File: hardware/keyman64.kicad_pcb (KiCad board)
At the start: 2 copper layers, 80 x 64.7 mm, 36 parts, among them J1 POWER, P1 COMPUTER, P2 KEYBOARD, P3 USB, P4 SERIAL, P5 CONTROL, SW1 RESET, SW2 BOOT, U1 CD74HC22106/MT8808, U2 ATMEGA1284P-PU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

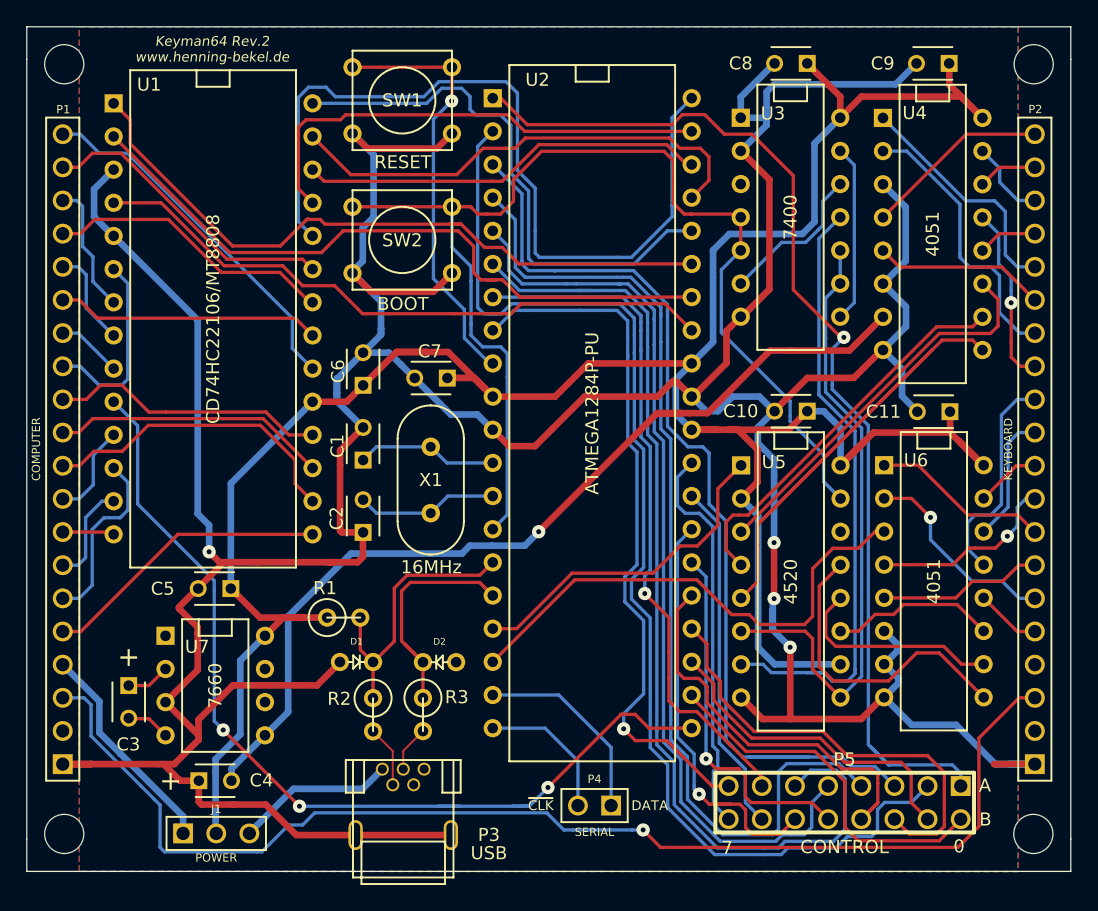
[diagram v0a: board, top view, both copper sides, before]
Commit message: Hardware: Increased mounting hole size to 4mm
This was self-adhesive pcb holders like reichelts AHS 4,8 may be used
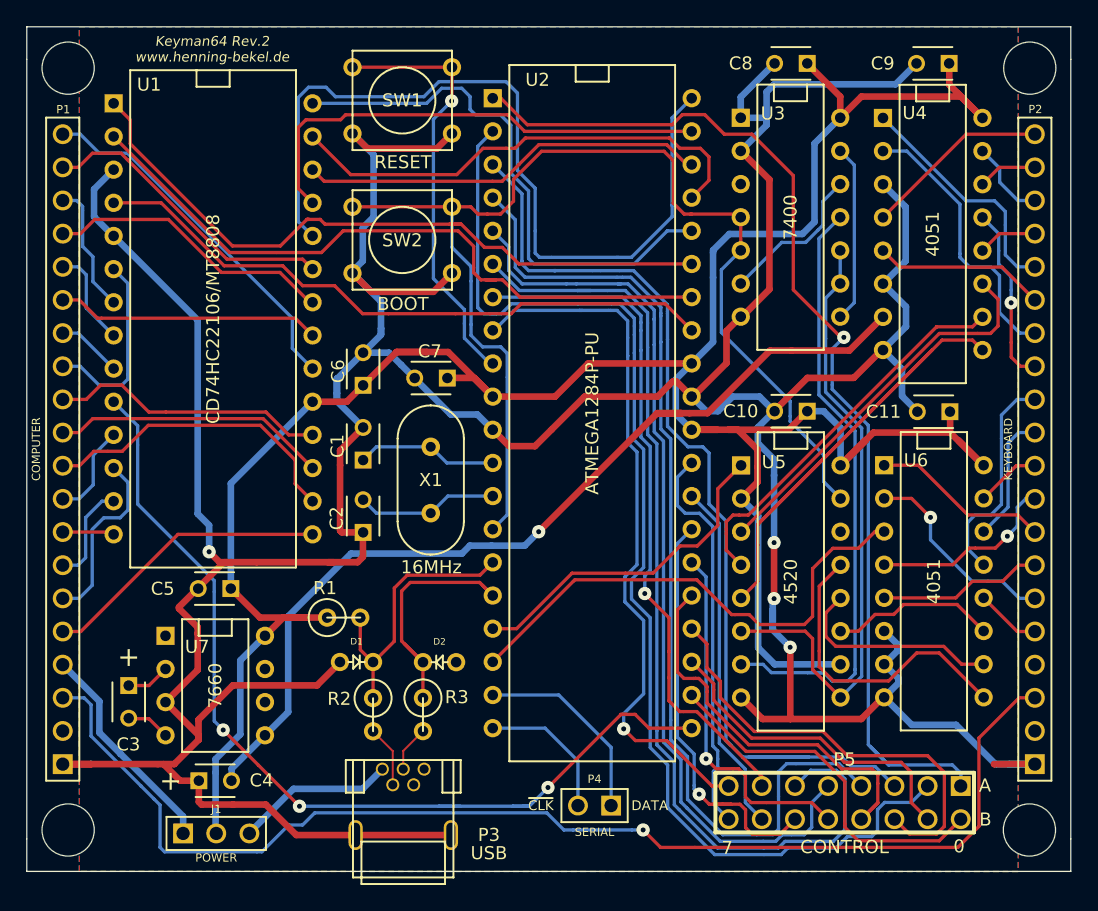
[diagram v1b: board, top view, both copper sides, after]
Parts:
- H1, H2, H3, H4: footprint Mounting_Holes:MountingHole_3mm -> Mounting_Holes:MountingHole_4mm
- moved H4 0.42 mm to (181.5, 69.5), turned to 180 degrees
- moved H1 0.42 mm to (107.8, 127.9)
- moved H3 0.42 mm to (107.8, 69.5)
- moved H2 0.42 mm to (181.4, 127.9)
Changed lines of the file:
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@@
     (area 104.572599 66.320199 184.657201 131.126701)
     (thickness 1.6)
-    (drawings 20)
+    (drawings 19)
     (tracks 1192)
     (zones 0)
@@
     (mod_text_size 1 1)
     (mod_text_width 0.15)
-    (pad_size 3.2 3.2)
-    (pad_drill 3.2)
+    (pad_size 4 4)
+    (pad_drill 4)
     (pad_to_mask_clearance 0)
     (aux_axis_origin 0 0)
@@
     (add_net /D-)
   )
-  (module Mounting_Holes:MountingHole_3mm (layer F.Cu)
-    (at 107.4928 128.2065)
-    (descr "Mounting hole, Befestigungsbohrung, 3mm, No Annular, Kein Restring,")
-    (tags "Mounting hole, Befestigungsbohrung, 3mm, No Annular, Kein Restring,")
-    (fp_text reference H1 (at 0.1524 -0.1778) (layer Dwgs.User) hide
-      (effects (font (size 1 1) (thickness 0.15)))
-    )
-    (fp_text value CONN_1 (at 1.00076 5.00126) (layer Dwgs.User) hide
-      (effects (font (size 1 1) (thickness 0.15)))
-    )
-    (fp_circle (center 0 0) (end 3 0) (layer Cmts.User) (width 0.381))
-    (pad 1 thru_hole circle (at 0 0) (size 3 3) (drill 3) (layers)
-      (net 83 "Net-(H1-Pad1)"))
-  )
-  (module Mounting_Holes:MountingHole_3mm (layer F.Cu)
-    (at 181.737 128.2065)
-    (descr "Mounting hole, Befestigungsbohrung, 3mm, No Annular, Kein Restring,")
-    (tags "Mounting hole, Befestigungsbohrung, 3mm, No Annular, Kein Restring,")
-    (fp_text reference H2 (at 0.1397 -0.1016) (layer Dwgs.User) hide
-      (effects (font (size 1 1) (thickness 0.15)))
-    )
-    (fp_text value CONN_1 (at 1.00076 5.00126) (layer Dwgs.User) hide
-      (effects (font (size 1 1) (thickness 0.15)))
-    )
-    (fp_circle (center 0 0) (end 3 0) (layer Cmts.User) (width 0.381))
-    (pad 1 thru_hole circle (at 0 0) (size 3 3) (drill 3) (layers)
-      (net 84 "Net-(H2-Pad1)"))
-  )
-  (module Mounting_Holes:MountingHole_3mm (layer F.Cu)
-    (at 107.4928 69.2404)
-    (descr "Mounting hole, Befestigungsbohrung, 3mm, No Annular, Kein Restring,")
-    (tags "Mounting hole, Befestigungsbohrung, 3mm, No Annular, Kein Restring,")
-    (fp_text reference H3 (at -0.0254 -0.0889) (layer Dwgs.User) hide
-      (effects (font (size 1 1) (thickness 0.15)))
-    )
-    (fp_text value CONN_1 (at -0.0254 -3.8354) (layer Dwgs.User) hide
-      (effects (font (size 1 1) (thickness 0.15)))
-    )
-    (fp_circle (center 0 0) (end 3 0) (layer Cmts.User) (width 0.381))
-    (pad 1 thru_hole circle (at 0 0) (size 3 3) (drill 3) (layers)
-      (net 85 "Net-(H3-Pad1)"))
-  )
-  (module Mounting_Holes:MountingHole_3mm (layer F.Cu)
-    (at 181.7624 69.2404)
-    (descr "Mounting hole, Befestigungsbohrung, 3mm, No Annular, Kein Restring,")
-    (tags "Mounting hole, Befestigungsbohrung, 3mm, No Annular, Kein Restring,")
-    (fp_text reference H4 (at 0.0762 -0.1397) (layer Dwgs.User) hide
-      (effects (font (size 1 1) (thickness 0.15)))
-    )
-    (fp_text value CONN_1 (at 0.3175 -4.0894) (layer Dwgs.User) hide
-      (effects (font (size 1 1) (thickness 0.15)))
-    )
-    (fp_circle (center 0 0) (end 3 0) (layer Cmts.User) (width 0.381))
-    (pad 1 thru_hole circle (at 0 0) (size 3 3) (drill 3) (layers)
-      (net 86 "Net-(H4-Pad1)"))
-  )
   (module Capacitors_ThroughHole:C_Disc_D3_P2.5 (layer F.Cu)
     (at 164.4142 69.1769 180)
@@
     )
   )
+  (module Mounting_Holes:MountingHole_4mm (layer F.Cu)
+    (at 107.7928 127.9065)
+    (descr "Mounting Hole 4mm, no annular")
+    (tags "mounting hole 4mm no annular")
+    (fp_text reference H1 (at 0.1572 6.5865) (layer F.SilkS) hide
+      (effects (font (size 1 1) (thickness 0.15)))
+    )
+    (fp_text value CONN_1 (at 0 5) (layer F.Fab)
+      (effects (font (size 1 1) (thickness 0.15)))
+    )
+    (fp_circle (center 0 0) (end 4 0) (layer Cmts.User) (width 0.15))
+    (fp_circle (center 0 0) (end 4.25 0) (layer F.CrtYd) (width 0.05))
+    (pad 1 np_thru_hole circle (at 0 0) (size 4 4) (drill 4) (layers *.Cu *.Mask F.SilkS)
+      (net 83 "Net-(H1-Pad1)"))
+  )
+  (module Mounting_Holes:MountingHole_4mm (layer F.Cu)
+    (at 181.437 127.9065)
+    (descr "Mounting Hole 4mm, no annular")
+    (tags "mounting hole 4mm no annular")
+    (fp_text reference H2 (at 0.173 6.5865) (layer F.SilkS) hide
+      (effects (font (size 1 1) (thickness 0.15)))
+    )
+    (fp_text value CONN_1 (at 0 5) (layer F.Fab)
+      (effects (font (size 1 1) (thickness 0.15)))
+    )
+    (fp_circle (center 0 0) (end 4 0) (layer Cmts.User) (width 0.15))
+    (fp_circle (center 0 0) (end 4.25 0) (layer F.CrtYd) (width 0.05))
+    (pad 1 np_thru_hole circle (at 0 0) (size 4 4) (drill 4) (layers *.Cu *.Mask F.SilkS)
+      (net 84 "Net-(H2-Pad1)"))
+  )
+  (module Mounting_Holes:MountingHole_4mm (layer F.Cu)
+    (at 107.7928 69.5404)
+    (descr "Mounting Hole 4mm, no annular")
+    (tags "mounting hole 4mm no annular")
+    (fp_text reference H3 (at 0 -5) (layer F.SilkS) hide
+      (effects (font (size 1 1) (thickness 0.15)))
+    )
+    (fp_text value CONN_1 (at 0 5) (layer F.Fab)
+      (effects (font (size 1 1) (thickness 0.15)))
+    )
+    (fp_circle (center 0 0) (end 4 0) (layer Cmts.User) (width 0.15))
+    (fp_circle (center 0 0) (end 4.25 0) (layer F.CrtYd) (width 0.05))
+    (pad 1 np_thru_hole circle (at 0 0) (size 4 4) (drill 4) (layers *.Cu *.Mask F.SilkS)
+      (net 85 "Net-(H3-Pad1)"))
+  )
+  (module Mounting_Holes:MountingHole_4mm (layer F.Cu)
+    (at 181.4624 69.5404 180)
+    (descr "Mounting Hole 4mm, no annular")
+    (tags "mounting hole 4mm no annular")
+    (fp_text reference H4 (at -0.0206 6.4214 180) (layer F.SilkS) hide
+      (effects (font (size 1 1) (thickness 0.15)))
+    )
+    (fp_text value CONN_1 (at 0 5 180) (layer F.Fab)
+      (effects (font (size 1 1) (thickness 0.15)))
+    )
+    (fp_circle (center 0 0) (end 4 0) (layer Cmts.User) (width 0.15))
+    (fp_circle (center 0 0) (end 4.25 0) (layer F.CrtYd) (width 0.05))
+    (pad 1 np_thru_hole circle (at 0 0 180) (size 4 4) (drill 4) (layers *.Cu *.Mask F.SilkS)
+      (net 86 "Net-(H4-Pad1)"))
+  )
   (dimension 79.9846 (width 0.3) (layer Dwgs.User)
     (gr_text "79,985 mm" (at 144.6149 58.936901) (layer Dwgs.User)
@@
     (effects (font (size 1.5 1.5) (thickness 0.3)))
   )
-  (gr_line (start 107.8992 73.3171) (end 107.8865 73.3044) (angle 90) (layer Dwgs.User) (width 0.2))
   (gr_line (start 184.6072 131.0767) (end 184.6072 128.5875) (angle 90) (layer Edge.Cuts) (width 0.1))
   (gr_line (start 104.6226 131.0767) (end 184.6072 131.0767) (angle 90) (layer Edge.Cuts) (width 0.1))
@@
     (effects (font (size 1 1) (thickness 0.15)))
   )
-  (gr_text "Keyman64 Rev.2 \nwww.henning-bekel.de" (at 118.8339 68.0847) (layer F.SilkS)
+  (gr_text "Keyman64 Rev.2\nwww.henning-bekel.de" (at 118.8339 68.0847) (layer F.SilkS)
     (effects (font (size 0.75 0.75) (thickness 0.15) italic))
   )

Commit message: Hardware: Improved silkscreen, added pin numbers at keyboard connectors
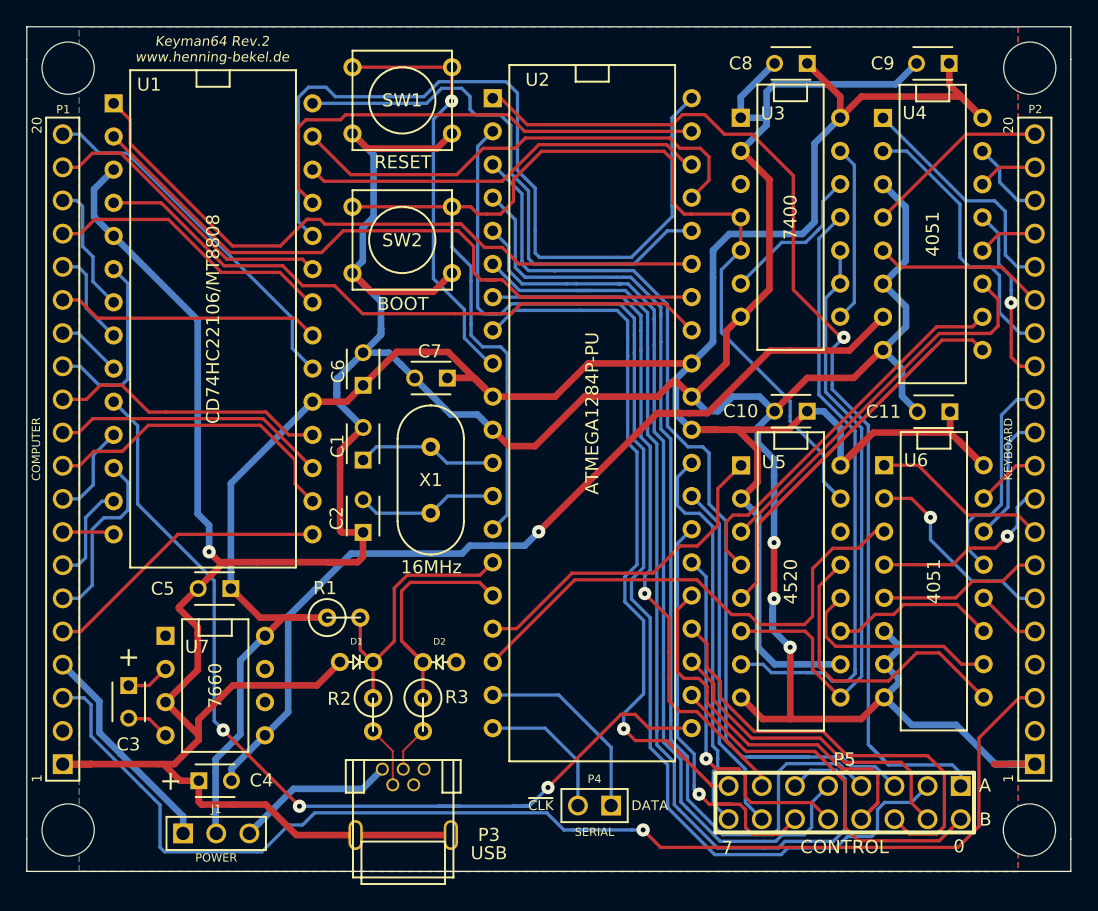
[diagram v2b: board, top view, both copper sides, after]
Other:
- board text added: "1"
- board text added: "20"
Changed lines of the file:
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@@
     (area 104.572599 66.320199 184.657201 131.126701)
     (thickness 1.6)
-    (drawings 19)
+    (drawings 23)
     (tracks 1192)
     (zones 0)
@@
       (net 86 "Net-(H4-Pad1)"))
   )
+  (gr_text 20 (at 179.832 73.914 90) (layer F.SilkS)
+    (effects (font (size 0.75 0.75) (thickness 0.15)))
+  )
+  (gr_text 1 (at 179.832 123.952 90) (layer F.SilkS)
+    (effects (font (size 0.75 0.75) (thickness 0.15)))
+  )
+  (gr_text 20 (at 105.41 73.914 90) (layer F.SilkS)
+    (effects (font (size 0.75 0.75) (thickness 0.15)))
+  )
+  (gr_text 1 (at 105.41 123.952 90) (layer F.SilkS)
+    (effects (font (size 0.75 0.75) (thickness 0.15)))
+  )
   (dimension 79.9846 (width 0.3) (layer Dwgs.User)

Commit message: Hardware: Improved routing, silkscreen
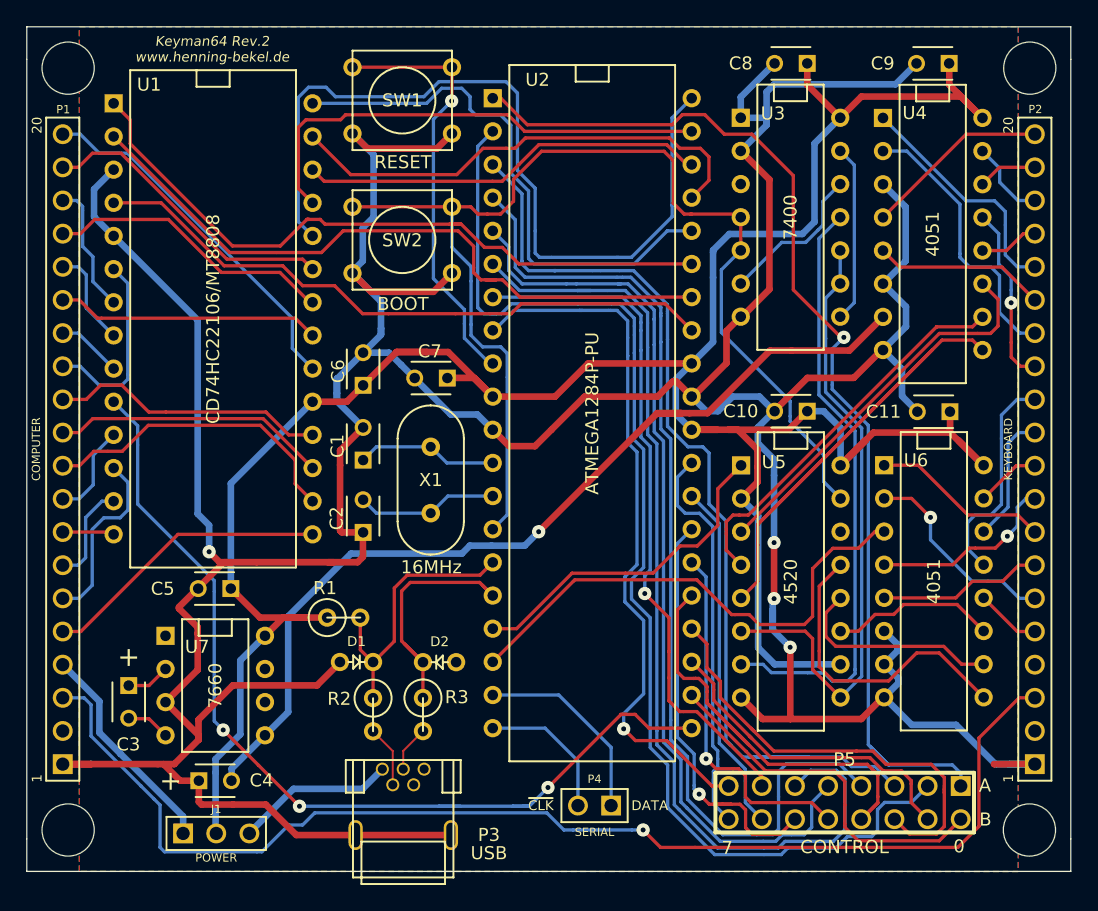
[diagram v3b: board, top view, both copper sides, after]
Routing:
- net /UB3: track 31.4 -> 36.7 mm
- net /UB2: track 34.4 -> 35.1 mm

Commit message: Hardware: Removed useless 7660, added alternative plcc-socket for mt8808
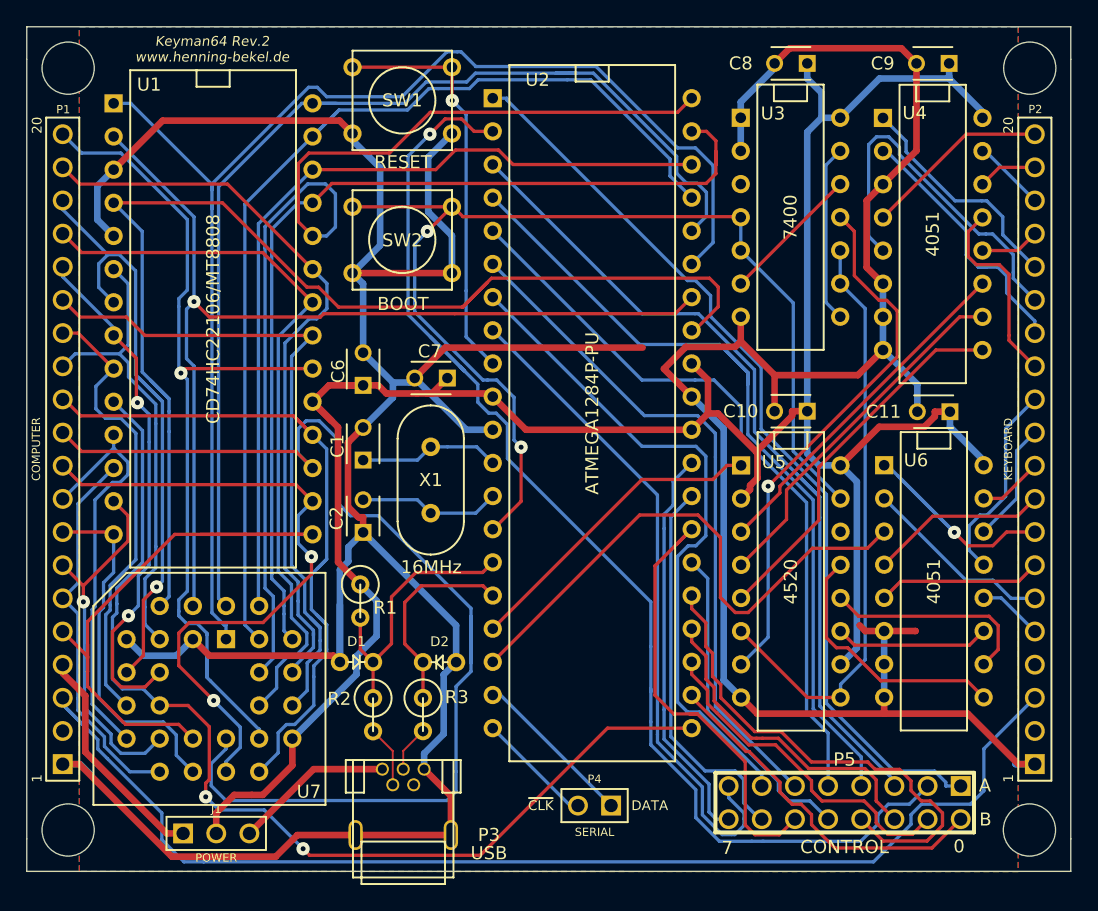
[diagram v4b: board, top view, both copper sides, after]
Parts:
- removed C3, C4: 10uF, Capacitors_ThroughHole:C_Disc_D3_P2.5
- removed C5: 100nF, Capacitors_ThroughHole:C_Disc_D3_P2.5
- U7: value 7660 -> CD74HC22106/MT8808; footprint Sockets_DIP:DIP-8__300 -> Sockets:PLCC28
- moved R1 1.80 mm to (130.2, 110.4), turned to 270 degrees
- moved U7 0.51 mm to (118.6, 117.1), turned to 0 degrees
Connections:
- U4 pad 7: /VEE -> GND
- U7 pad 1: (no net) -> /CPA5
- U7 pad 2: Net-(C3-Pad1) -> /~CPS
- U7 pad 4: Net-(C3-Pad2) -> /CPD
- U7 pad 5: /VEE -> GND
- U7 pad 6: Net-(U7-Pad6) -> /A0
- U7 pad 7: Net-(U7-Pad7) -> /A2
- U7 pad 8: VCC -> /A4
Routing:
- net /VEE: track 71.8 -> 0.00 mm, vias 1 -> 0
- net /B1: track 21.1 -> 87.7 mm
- net /CPA5: track 53.3 -> 101.5 mm
- net /CPD: track 49.0 -> 92.7 mm
- net /CPA4: track 41.9 -> 85.0 mm
- net /CPA3: track 37.0 -> 79.1 mm
- net /A7: track 27.9 -> 68.6 mm, vias 0 -> 1
- net /A2: track 10.0 -> 47.9 mm, vias 0 -> 1
- net /CPA2: track 31.2 -> 65.3 mm
- net /A1: track 23.3 -> 57.1 mm
- net /A3: track 22.2 -> 56.0 mm
- net /B0: track 21.2 -> 53.9 mm
- net /A5: track 20.3 -> 52.7 mm
- net /A4: track 7.57 -> 39.8 mm, vias 0 -> 2
- net /CPA1: track 41.7 -> 73.9 mm
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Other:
- board text removed: "+"

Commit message: Hardware: Rerouting in progress...
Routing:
- net Net-(D2-Pad1): track 16.0 -> 19.7 mm
- net /UB0: track 27.4 -> 30.3 mm
- net Net-(D1-Pad1): track 21.0 -> 23.9 mm
- net GND: track 345.6 -> 347.9 mm
- net /UB2: track 24.8 -> 26.8 mm
- net /UB5: track 34.6 -> 35.8 mm
- net /UB1: track 26.1 -> 26.9 mm
- net /UB3: track 38.2 -> 38.9 mm

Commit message: Hardware: Rerouting in progress...
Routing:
- net /UA1: track 93.3 -> 128.0 mm
- net VCC: track 180.0 -> 190.8 mm
- net /CRES: track 41.4 -> 48.9 mm
- net /UB4: track 24.9 -> 32.3 mm
- net /UA0: track 71.0 -> 76.3 mm
- net /UA5: track 52.0 -> 56.6 mm
- net /B5: track 28.1 -> 32.3 mm
- net GND: track 347.9 -> 351.3 mm
- net /UA6: track 51.1 -> 53.8 mm
- net /A2: track 47.9 -> 50.4 mm
- net /B7: track 31.8 -> 34.2 mm
- net /C0: track 15.0 -> 17.0 mm
- net Net-(U3-Pad13): track 13.6 -> 15.6 mm
- net /A3: track 56.0 -> 57.9 mm
- net /B2: track 51.8 -> 53.6 mm
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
